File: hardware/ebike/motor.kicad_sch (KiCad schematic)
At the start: 0 parts

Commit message: first draft of motor control circuitry, need to annotate still
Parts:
- added C32, C33, C34: 2.2u, symbol Device:C
- added C35, C36: 1n, symbol Device:C
- added D3, D4, D5: D_TVS, symbol Device:D_TVS
- added Q2, Q3, Q4, Q5, Q6, Q7: IPD30N10S3L34ATMA1, symbol Simulation_SPICE:NMOS
- added R10, R11, R12, R13, R14, R9: 10, symbol Device:R
- added R15, R18, R20: 39k, symbol Device:R
- added R16, R17, R19: 2k2, symbol Device:R
- added R7, R8: 10m, symbol Device:R_Shunt
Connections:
- new net: Q2.2 (G), R9.1
- new net: Q3.2 (G), R11.1
- new net: Q6.2 (G), R12.1
- new net: Q7.2 (G), R14.1
- new net: Q4.2 (G), R13.1
- new net: Q5.2 (G), R10.1
- new net GND: C32.2, C33.2, C34.2, D3.2 (A2), D4.2 (A2), D5.2 (A2), Q7.3 (S), R16.1, R17.1, R19.1, R7.4, R8.4
- new net G_H1: R9.2
- new net G_H2: R11.2, R13.2
- new net G_L1: R10.2
- new net G_L2: R12.2, R14.2
- new net H1_VS: Q2.3 (S), Q5.1 (D), R18.2
- new net H2_VS: Q3.3 (S), Q6.1 (D), R15.2
- new net H3_VS: Q4.3 (S), Q7.1 (D), R20.2
- new net L1_VS: Q5.3 (S), R7.1
- new net L2_VS: Q6.3 (S), R8.1
- new net SENSE1: D4.1 (A1), R17.2, R18.1
- new net SENSE2: D3.1 (A1), R15.1, R16.2
- new net SENSE3: D5.1 (A1), R19.2, R20.1
- new net SHUNT1_A: C35.2, R7.2
- new net SHUNT1_B: C35.1, R7.3
- new net SHUNT2_A: C36.2, R8.2
- new net SHUNT2_B: C36.1, R8.3
- new net VBAT+: C32.1, C33.1, C34.1, Q2.1 (D), Q3.1 (D), Q4.1 (D)
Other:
- note added: "Double check resistor values, these should be good but double check"
- note added: "MOSFET 3 phase half-bridges"
- note added: "TODO: Add HAL sensor circuitry"
- note added: "TODO: Add regenerative braking circuitry"
- note added: "Voltage Sensing"

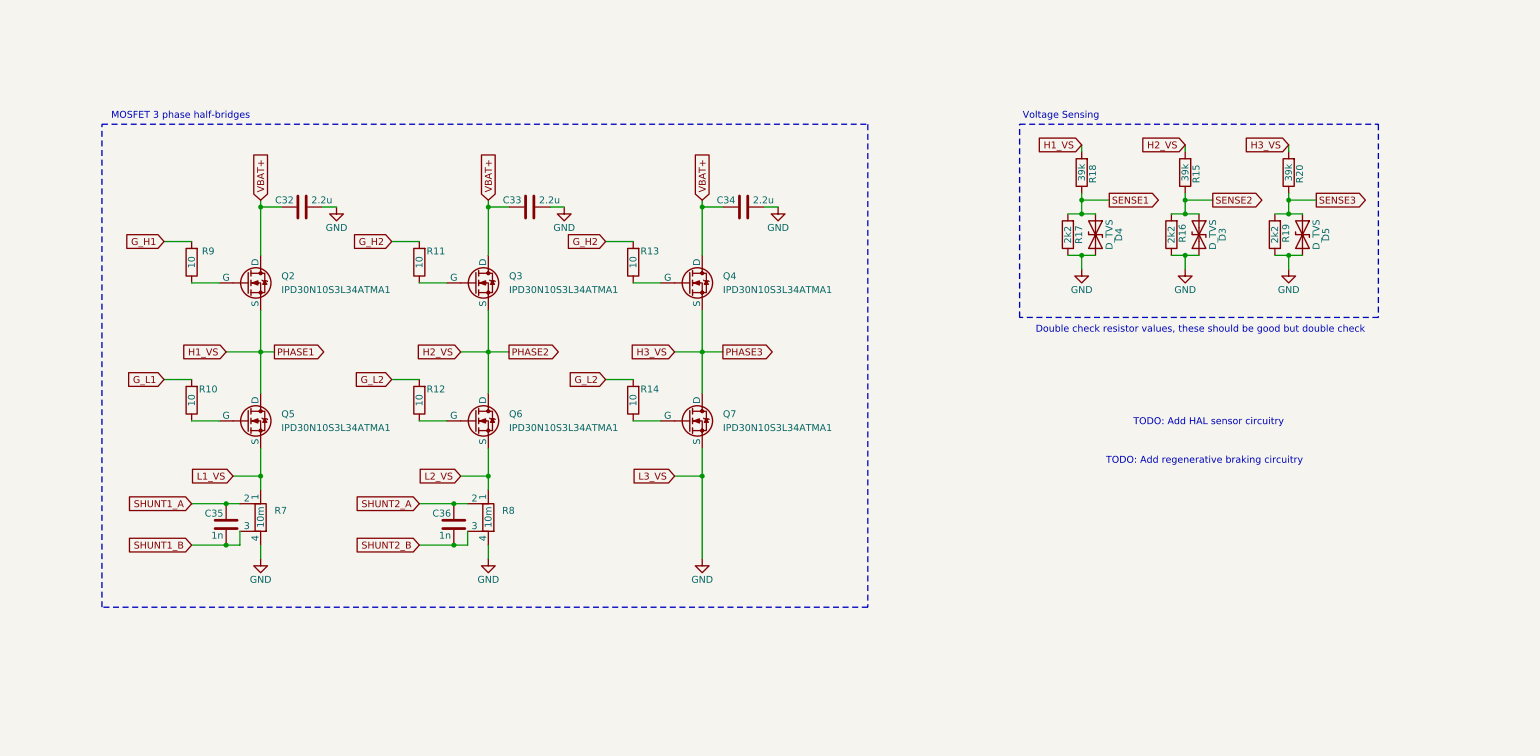
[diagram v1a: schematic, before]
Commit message: Wired PWM, ADC to MCU. Added HAL filtration + battery decoupling
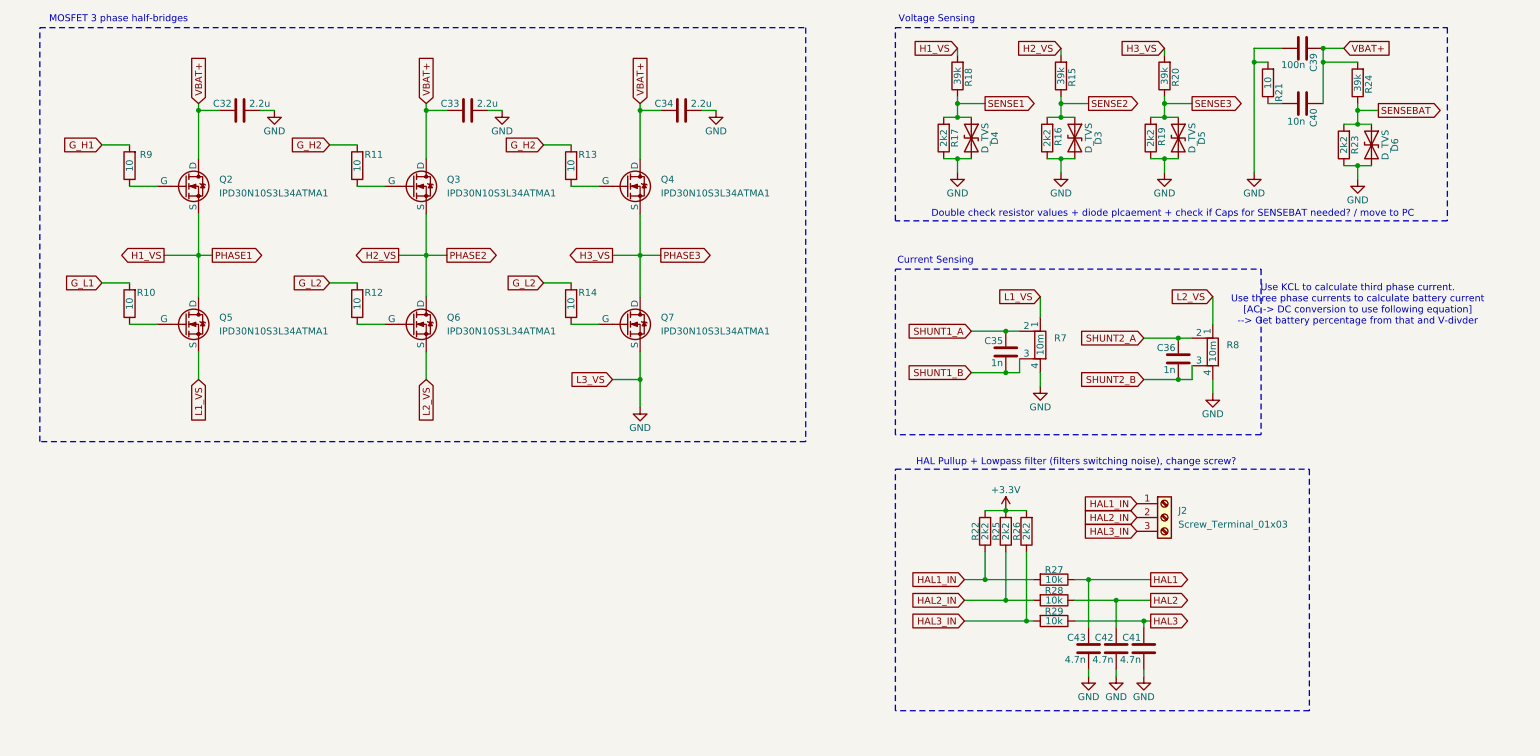
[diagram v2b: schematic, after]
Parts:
- added C39: 100n, symbol Device:C
- added C40: 10n, symbol Device:C
- added C41, C42, C43: 4.7n, symbol Device:C
- added D6: D_TVS, symbol Device:D_TVS
- added J2: Screw_Terminal_01x03, symbol Connector:Screw_Terminal_01x03
- added R21: 10, symbol Device:R
- added R22, R23, R25, R26: 2k2, symbol Device:R
- added R24: 39k, symbol Device:R
- added R27, R28, R29: 10k, symbol Device:R
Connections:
- net GND: now also C39.1, C41.1, C42.1, C43.1, D6.2 (A2), R21.2, R23.1
- net VBAT+: now also C39.2, C40.2, R24.2
- new net: C40.1, R21.1
- new net +3.3V: R22.2, R25.2, R26.2
- new net HAL1: C43.2, R27.1
- new net HAL1_IN: J2.1 (Pin_1), R22.1, R27.2
- new net HAL2: C42.2, R28.1
- new net HAL2_IN: J2.2 (Pin_2), R25.1, R28.2
- new net HAL3: C41.2, R29.1
- new net HAL3_IN: J2.3 (Pin_3), R26.1, R29.2
- new net SENSEBAT: D6.1 (A1), R23.2, R24.1
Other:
- note added: "Current Sensing"
- note added: "Double check resistor values + diode plcaement + check if Caps for SENSEBAT needed? / move to PC"
- note added: "HAL Pullup + Lowpass filter (filters switching noise), change screw?"
- note added: "Use KCL to calculate third phase current. Use three phase currents to calculate battery current [AC -> DC conversion to use following equation] --> Get battery percentage from that and V-divder"
- note removed: "Double check resistor values, these should be good but double check"
- note removed: "TODO: Add HAL sensor circuitry"
- note removed: "TODO: Add regenerative braking circuitry"
- moved on the sheet: C32, C33, C34, C35, C36, D3, D4, D5, Q2, Q3, Q4, Q5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

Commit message: schematic ready for first review
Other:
- note added: "Place caps near STM"
- note added: "Remove 2.2? / place these in the PC"
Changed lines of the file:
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@@
+		)
+	)
+	(text "Place caps near STM"
+		(exclude_from_sim no)
+		(at 231.648 131.064 0)
+		(effects
+			(font
+				(size 1.27 1.27)
+			)
 		)
 	)
@@
 		(effects
 			(font
+				(size 1.27 1.27)
+			)
+		)
+	)
+	(text "Remove 2.2? / place these in the PC"
+		(exclude_from_sim no)
+		(at 68.58 23.876 0)
+		(effects
+			(font

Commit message: working through first review, edited Power control a lot
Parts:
- added R42, R43, R44, R45: 100, symbol Device:R
- Q2, Q3, Q4, Q5, Q6, Q7: value IPD30N10S3L34ATMA1 -> CSD19532KTT
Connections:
- net SHUNT1_A: now also R42.1; no longer C35.2, R7.2
- net SHUNT1_B: now also R43.1; no longer C35.1, R7.3
- net SHUNT2_A: now also R44.1; no longer C36.2, R8.2
- net SHUNT2_B: now also R45.1; no longer C36.1, R8.3
- new net: C35.2, R42.2, R7.2
- new net: C35.1, R43.2, R7.3
- new net: C36.2, R44.2, R8.2
- new net: C36.1, R45.2, R8.3
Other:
- note added: "2.2 DC-Link decoupling"
- note added: "Use KCL to calculate third phase current. Use three phase currents to calculate battery current [AC -> DC conversion to use following equation] --> Get battery percentage from that and V-divder ****** Maybe add third sense, b/c this assume that current only goes through motor (maybe not?) ^^ Look into this"
- note removed: "Remove 2.2? / place these in the PC"
- note removed: "Use KCL to calculate third phase current. Use three phase currents to calculate battery current [AC -> DC conversion to use following equation] --> Get battery percentage from that and V-divder"
- moved on the sheet: C35, R7

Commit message: finished annoation for schematic
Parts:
- removed C40: 10n, symbol Device:C
- removed R21: 10, symbol Device:R
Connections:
- net SENSEBAT: now also C39.2
- net VBAT+: no longer C39.2
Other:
- note added: "Check current going into these, could fry DRV"
- note added: "Use KCL to calculate third phase current. Use three phase currents to estimate battery current [AC -> DC conversion to use following equation] --> Get battery percentage from that and V-divder"
- note removed: "Double check resistor values + diode plcaement + check if Caps for SENSEBAT needed? / move to PC"
- note removed: "Use KCL to calculate third phase current. Use three phase currents to calculate battery current [AC -> DC conversion to use following equation] --> Get battery percentage from that and V-divder ****** Maybe add third sense, b/c this assume that current only goes through motor (maybe not?) ^^ Look into this"
- moved on the sheet: C35, C36, C39, C41, C42, C43, D3, D4, D5, D6, J2, R15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

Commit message: minor fixes
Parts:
- removed D3, D4, D5, D6: D_TVS, symbol Device:D_TVS
- added C40, C50, C52: .1u, symbol Device:C
- added D2, D3, D4: D_Schottky, symbol Device:D_Schottky
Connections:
- net +3.3V: now also D2.1 (K), D3.1 (K), D4.1 (K)
- net GND: now also C40.2, C50.2, C52.2
- net SENSE1: now also C40.1, D2.2 (A)
- net SENSE2: now also C50.1, D4.2 (A)
- net SENSE3: now also C52.1, D3.2 (A)
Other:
- note added: "Place cap close to pins on DRV"
- note removed: "Check current going into these, could fry DRV"
- moved on the sheet: R15, R16, R18, R19, R20, R23, R24

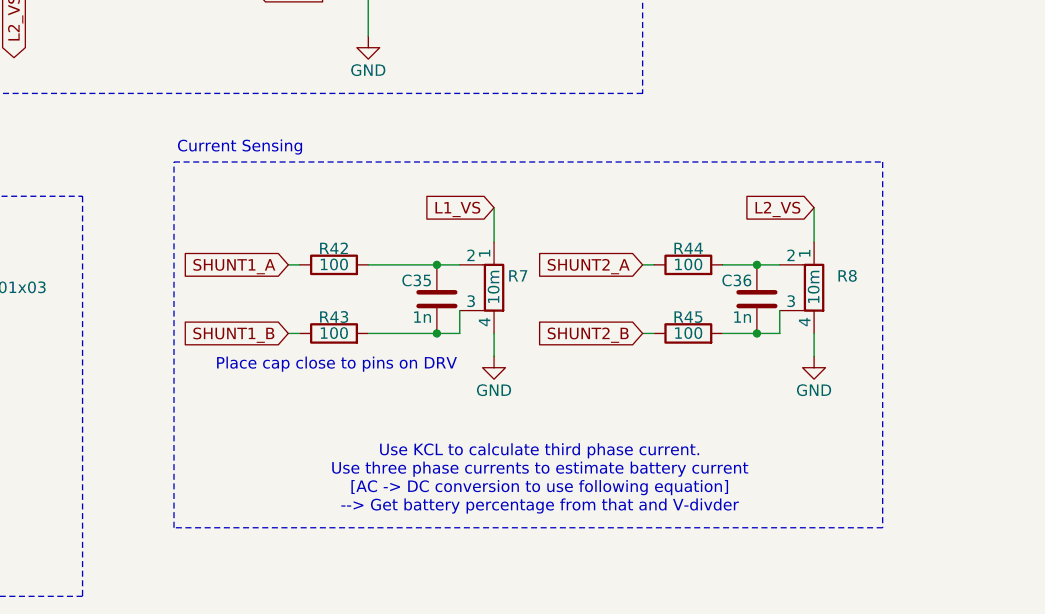
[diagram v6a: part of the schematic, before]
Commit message: started working on footprint assignment
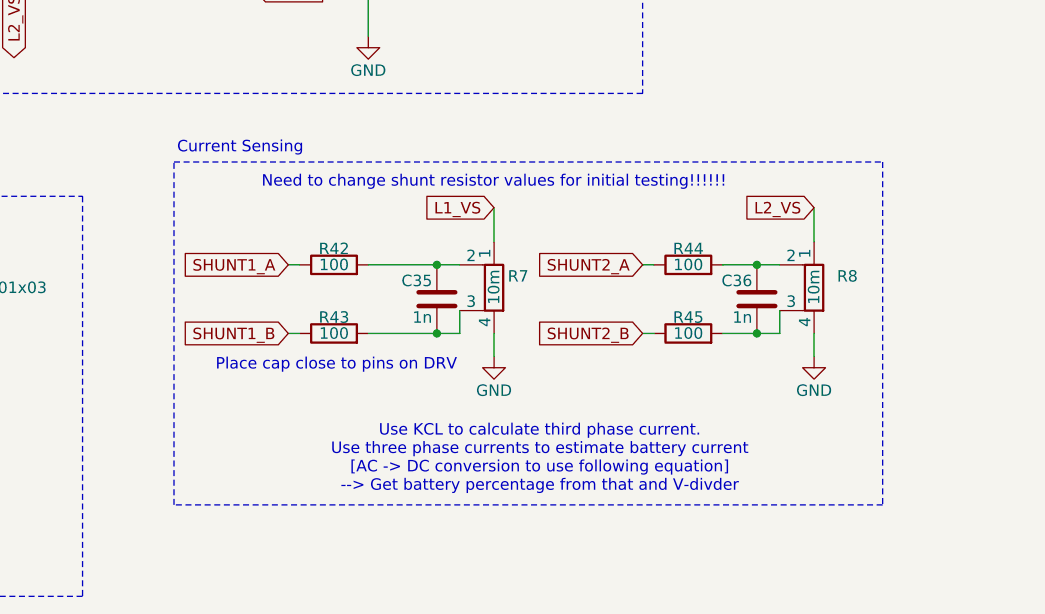
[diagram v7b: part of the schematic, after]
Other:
- note added: "Need to change shunt resistor values for initial testing!!!!!!"
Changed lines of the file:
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@@
 	(rectangle
 		(start 105.41 102.87)
-		(end 184.15 143.51)
+		(end 184.15 140.97)
 		(stroke
 			(width 0)
@@
 		)
 	)
+	(text "Need to change shunt resistor values for initial testing!!!!!!\n"
+		(exclude_from_sim no)
+		(at 140.97 105.156 0)
+		(effects
+			(font
+				(size 1.27 1.27)
+			)
+		)
+	)
 	(text "Place cap close to pins on DRV"
 		(exclude_from_sim no)
@@
 	(text "Use KCL to calculate third phase current.\nUse three phase currents to estimate battery current \n[AC -> DC conversion to use following equation]\n--> Get battery percentage from that and V-divder\n\n"
 		(exclude_from_sim no)
-		(at 146.05 139.192 0)
+		(at 146.05 136.906 0)
 		(effects
 			(font
@@
 			)
 		)
-		(property "Datasheet" "~"
+		(property "Datasheet" "https://www.digikey.com/en/products/detail/kemet/C0805C104KMREC7210/8645300"
 			(at 254 64.77 0)
 			(effects
